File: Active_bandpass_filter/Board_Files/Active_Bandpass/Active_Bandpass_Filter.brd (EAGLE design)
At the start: 100 x 80 mm, 25 parts, among them IC1 AD8542R, IC2 AD8031R, IC3 7805TV, IC4 AD8542R

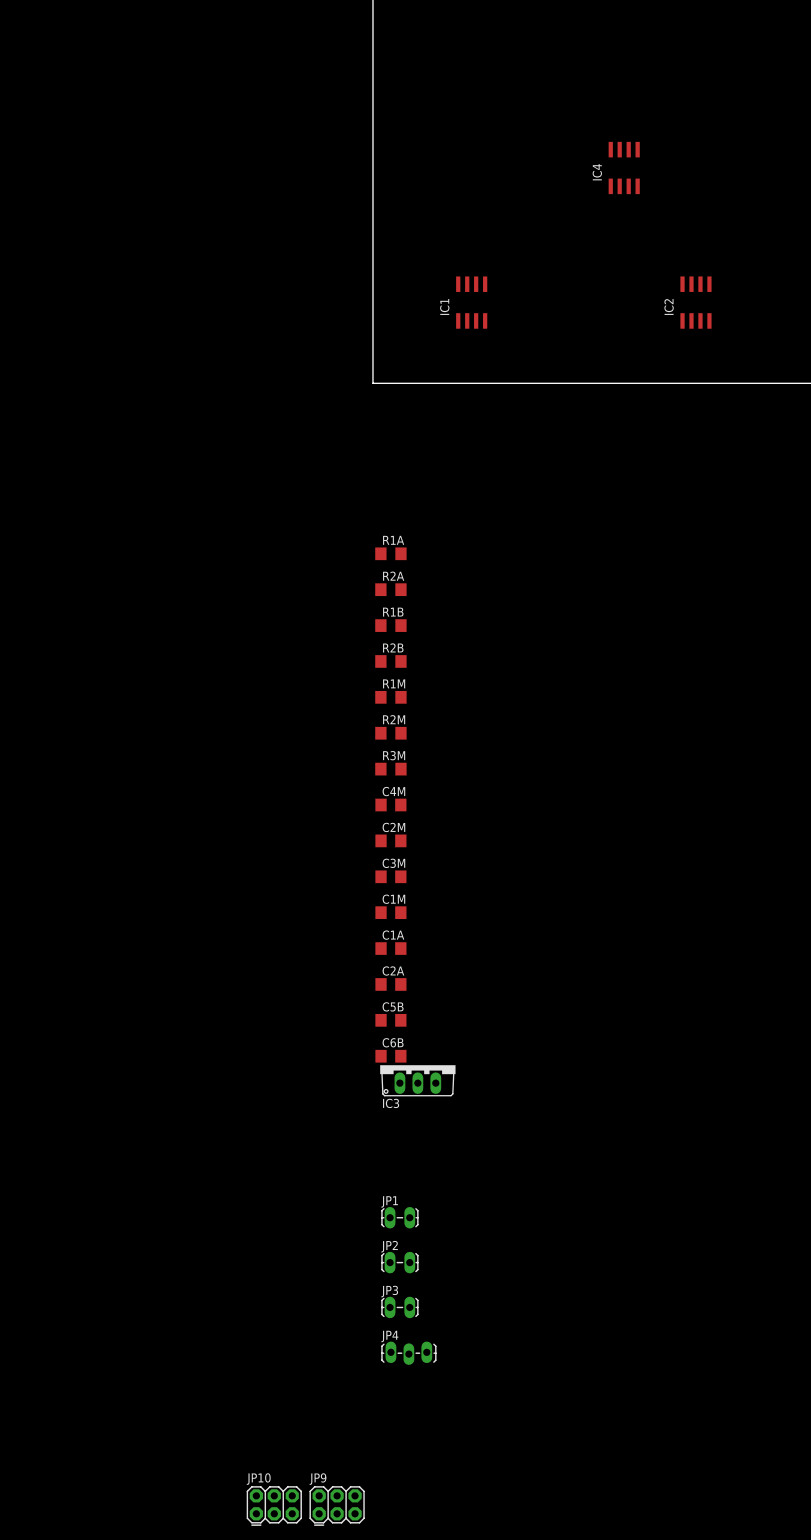
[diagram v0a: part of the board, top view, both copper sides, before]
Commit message: split into 2 boards
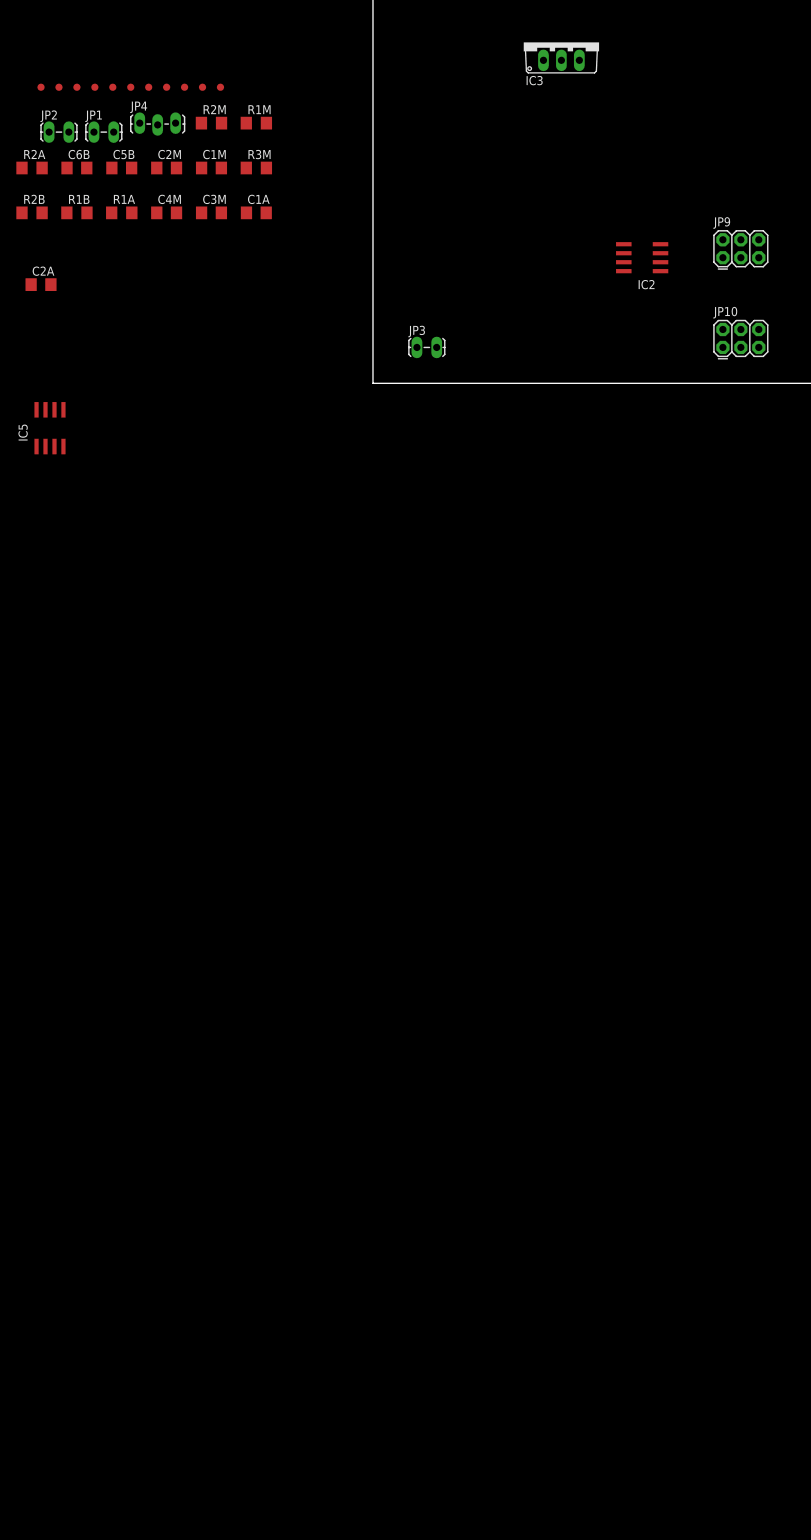
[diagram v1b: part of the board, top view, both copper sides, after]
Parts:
- removed IC1, IC4: AD8542R, analog-devices:SO8
- added IC5: AD8542R, analog-devices:SO8
- added TP1, TP10, TP11, TP2, TP3, TP4, TP5, TP6, TP7, TP8, TP9: TEST-POINT3X4, SparkFun-Passives:PAD.03X.04
- moved JP9 186.8 mm to (49.5, 17.8)
- moved JP10 177.8 mm to (49.5, 5.08)
- moved JP4 177.6 mm to (-33.0, 36.8)
- moved JP2 167.1 mm to (-45.7, 35.6)
- moved JP1 159.3 mm to (-39.4, 35.6)
- moved IC3 146.2 mm to (26.7, 48.3)
- moved JP3 135.9 mm to (6.35, 5.08)
- moved C6B 133.4 mm to (-41.9, 30.5)
- moved C5B 126.5 mm to (-35.6, 30.5)
- moved C2A 110.8 mm to (-47.0, 14.0)
- moved C1M 108.4 mm to (-22.9, 30.5)
- moved C1A 105.9 mm to (-16.5, 24.1)
- moved C2M 100.4 mm to (-29.2, 30.5)
- moved C3M 97.4 mm to (-22.9, 24.1)
- moved R2M 90.0 mm to (-22.9, 36.8)
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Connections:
- removed net N$7: C5B.1, IC4.1
- removed net V+: IC4.8
- removed net V-: IC4.4
- net 5V: now also IC5.8, TP10.P$1, TP6.P$1, TP9.P$1; no longer IC1.8
- net GND: now also IC5.4, TP11.P$1, TP7.P$1, TP8.P$1; no longer IC1.4
- net N$2: now also IC5.3; no longer IC4.3
- net N$3: now also C5B.1, IC5.1, IC5.2, TP1.P$1; no longer IC4.2
- net N$5: now also IC5.5; no longer IC4.5
- net REF: now also TP2.P$1, TP4.P$1
- net SIG_IN: now also TP3.P$1
- net SIG_OUT: now also IC5.6, IC5.7, TP5.P$1; no longer IC4.6, IC4.7
